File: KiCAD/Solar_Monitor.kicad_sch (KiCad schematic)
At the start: 10 parts, among them J1 Power IN, J2 Power Out, Q1 PN2222A, Q2 MCP102-300E/TO, U1 PIC16F15214-I/P

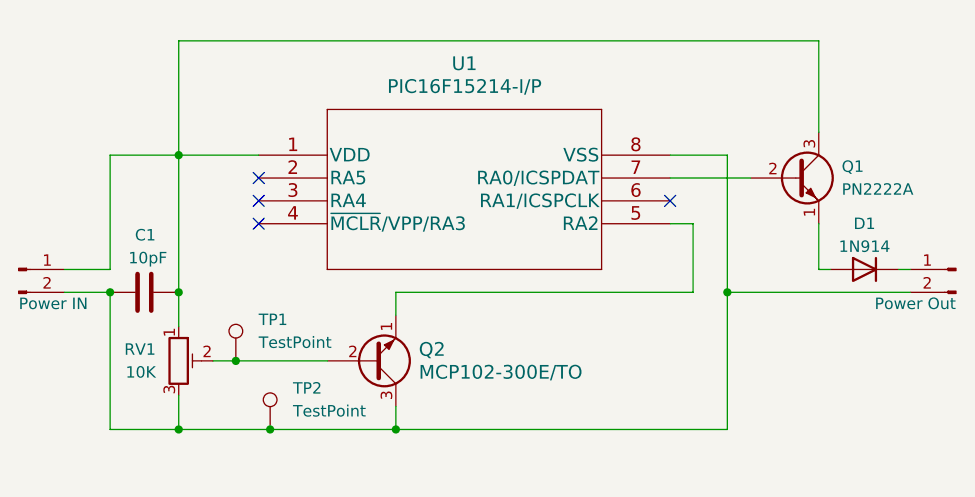
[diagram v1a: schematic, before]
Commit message: KiCAD: Added button
Added button to reset the output for a set amount of time.
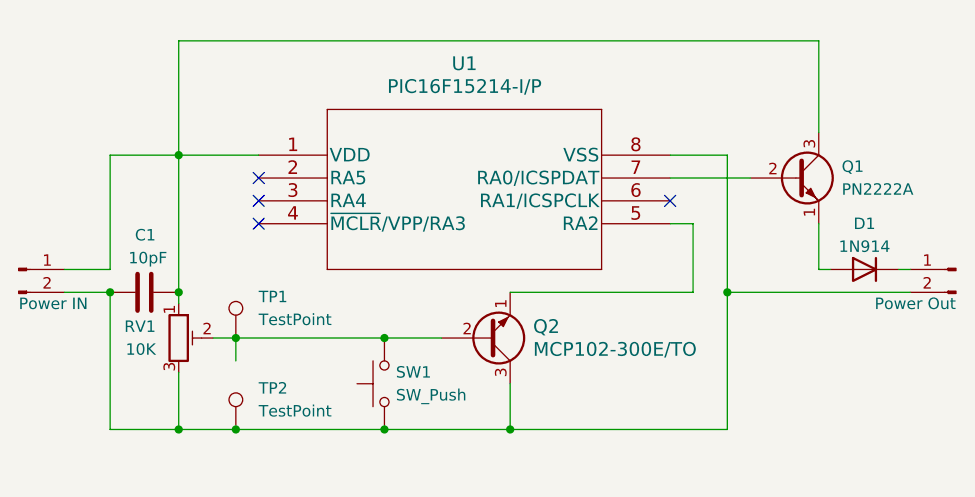
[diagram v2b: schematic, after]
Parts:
- added SW1: SW_Push, Button_Switch_THT:SW_PUSH_6mm, symbol Switch:SW_Push
- Q1: footprint Package_TO_SOT_THT:TO-92_Inline -> Package_TO_SOT_THT:TO-92
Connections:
- net at C1.1, J1.2 (Pin_2), J2.2 (Pin_2)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: now also SW1.1
- net at Q2.2, RV1.2, TP1.1: now also SW1.2
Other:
- moved on the sheet: Q2, RV1, TP1, TP2

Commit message: Moving on
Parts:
- Q2: value MCP102-300E/TO -> (none)
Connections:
- net -5v: now reaches C1.1, J1.2 (Pin_2), J2.2 (Pin_2), Q2.3, RV1.3, SW1.1, TP2.1, U1.8 (VSS)
- net +5v: now reaches C1.2, J1.1 (Pin_1), Q1.3 (C), RV1.1, U1.1 (VDD)
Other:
- note added: "TP1 + TP2 = 3.00volts"
- moved on the sheet: Q2, RV1, SW1, TP1, TP2

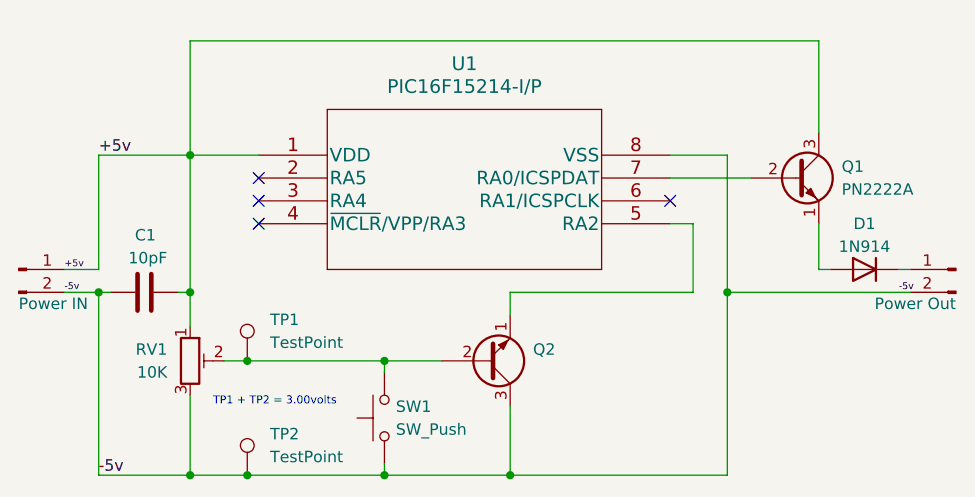
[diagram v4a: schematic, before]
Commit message: Switch to an ATTiny402
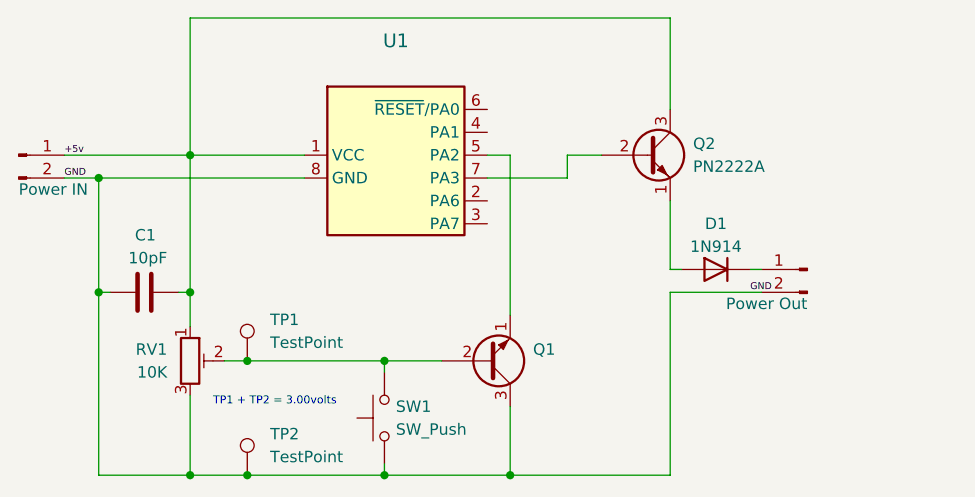
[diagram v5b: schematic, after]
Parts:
- removed U1: PIC16F15214-I/P, Package_DIP:DIP-8_W7.62mm_Socket, symbol PIC16F15214:PIC16F15214-I/P
- added U1: (no value), Package_SO:SOIC-8_3.9x4.9mm_P1.27mm, symbol MCU_Microchip_ATtiny:ATtiny202-SS
- renumbered Q2 to Q1, Q1 to Q2
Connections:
- net +5v: now also U1.1 (VCC)
- net at Q1.1: now also U1.5 (PA2)
- net at Q2.2 (B): now also U1.7 (PA3)
- net -5v renamed GND
- net GND: now also U1.8 (GND)
- no-connect marks 4 -> 0
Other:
- moved on the sheet: D1, Q2
